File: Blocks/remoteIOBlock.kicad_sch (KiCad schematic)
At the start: 1 part, among them IC44 PCA9555PW,118

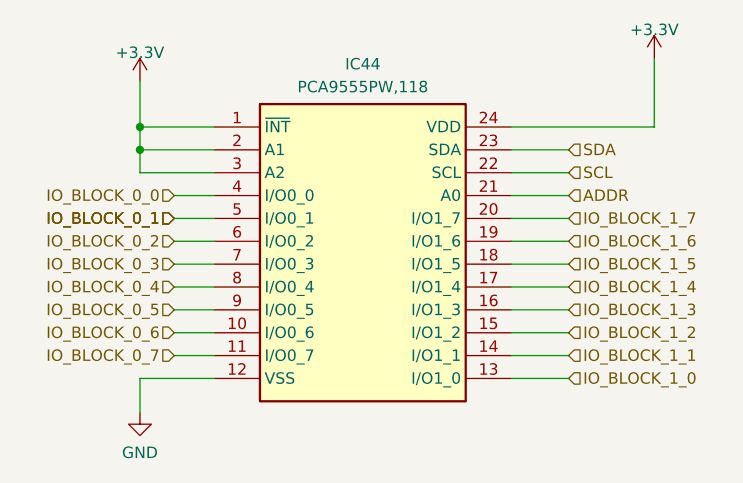
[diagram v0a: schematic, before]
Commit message: Automate library addition * Added script to automagically extract samacsys libraries and put them in corresponding folders. * Note: Requires zsh
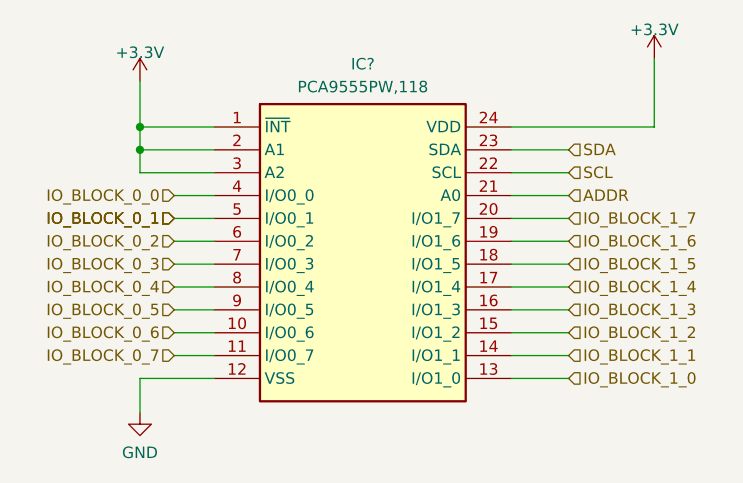
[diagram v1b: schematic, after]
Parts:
- IC?: renamed from IC44; footprint PCA9555PW,118:SOP65P640X110-24N -> PCA9555PW_118:SOP65P640X110-24N
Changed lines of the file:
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@@
   (symbol (lib_id "PCA9555PW_118:PCA9555PW,118") (at 129.54 83.185 0) (unit 1)
     (in_bom yes) (on_board yes) (dnp no) (fields_autoplaced)
-    (property "Reference" "IC44" (at 146.05 76.2 0)
+    (property "Reference" "IC?" (at 146.05 76.2 0)
       (effects (font (size 1.27 1.27)))
     )
@@
       (effects (font (size 1.27 1.27)))
     )
-    (property "Footprint" "PCA9555PW,118:SOP65P640X110-24N" (at 158.75 178.105 0)
+    (property "Footprint" "PCA9555PW_118:SOP65P640X110-24N" (at 158.75 178.105 0)
       (effects (font (size 1.27 1.27)) (justify left top) hide)
     )
@@
       (project "PLC-CIM"
         (path "/98f81d77-8880-491b-a7cf-4c27e2d73edf"
-          (reference "IC44") (unit 1)
+          (reference "IC?") (unit 1)
         )
         (path "/98f81d77-8880-491b-a7cf-4c27e2d73edf/35995f38-68c0-46e2-b2fd-985fe3f09ad0"
@@
   (symbol (lib_id "power:+3.3V") (at 178.435 75.565 0) (unit 1)
     (in_bom yes) (on_board yes) (dnp no) (fields_autoplaced)
-    (property "Reference" "#PWR0118" (at 178.435 79.375 0)
+    (property "Reference" "#PWR0274" (at 178.435 79.375 0)
       (effects (font (size 1.27 1.27)) hide)
     )
@@
       (project "PLC-CIM"
         (path "/98f81d77-8880-491b-a7cf-4c27e2d73edf/35995f38-68c0-46e2-b2fd-985fe3f09ad0"
-          (reference "#PWR0118") (unit 1)
+          (reference "#PWR0274") (unit 1)
         )
         (path "/98f81d77-8880-491b-a7cf-4c27e2d73edf/be2e0416-3be1-412f-8c3d-deda81998237"
-          (reference "#PWR0123") (unit 1)
+          (reference "#PWR0277") (unit 1)
         )
       )
@@
   (symbol (lib_id "power:+3.3V") (at 121.285 78.105 0) (unit 1)
     (in_bom yes) (on_board yes) (dnp no) (fields_autoplaced)
-    (property "Reference" "#PWR0119" (at 121.285 81.915 0)
+    (property "Reference" "#PWR0275" (at 121.285 81.915 0)
       (effects (font (size 1.27 1.27)) hide)
     )
@@
       (project "PLC-CIM"
         (path "/98f81d77-8880-491b-a7cf-4c27e2d73edf/35995f38-68c0-46e2-b2fd-985fe3f09ad0"
-          (reference "#PWR0119") (unit 1)
+          (reference "#PWR0275") (unit 1)
         )
         (path "/98f81d77-8880-491b-a7cf-4c27e2d73edf/be2e0416-3be1-412f-8c3d-deda81998237"
-          (reference "#PWR0121") (unit 1)
+          (reference "#PWR0278") (unit 1)
         )
       )
@@
   (symbol (lib_id "power:GND") (at 121.285 114.935 0) (unit 1)
     (in_bom yes) (on_board yes) (dnp no) (fields_autoplaced)
-    (property "Reference" "#PWR0120" (at 121.285 121.285 0)
+    (property "Reference" "#PWR0276" (at 121.285 121.285 0)
       (effects (font (size 1.27 1.27)) hide)
     )
@@
       (project "PLC-CIM"
         (path "/98f81d77-8880-491b-a7cf-4c27e2d73edf/35995f38-68c0-46e2-b2fd-985fe3f09ad0"
-          (reference "#PWR0120") (unit 1)
+          (reference "#PWR0276") (unit 1)
         )
         (path "/98f81d77-8880-491b-a7cf-4c27e2d73edf/be2e0416-3be1-412f-8c3d-deda81998237"
-          (reference "#PWR0122") (unit 1)
+          (reference "#PWR0279") (unit 1)
         )
       )
